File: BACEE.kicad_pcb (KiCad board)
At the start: 2 copper layers, 42.7 x 24.4 mm, 17 parts, among them J2 I2C connector, J3 Digital pins, J4 Serial connector, J5 ICSP connector, U1 24LC1025, U2 DS1337S+, U3 24LC1025, U4 ATMEGA328P-AU, Y1 Crystal32768KHz, Y2 Crystal 16MHz

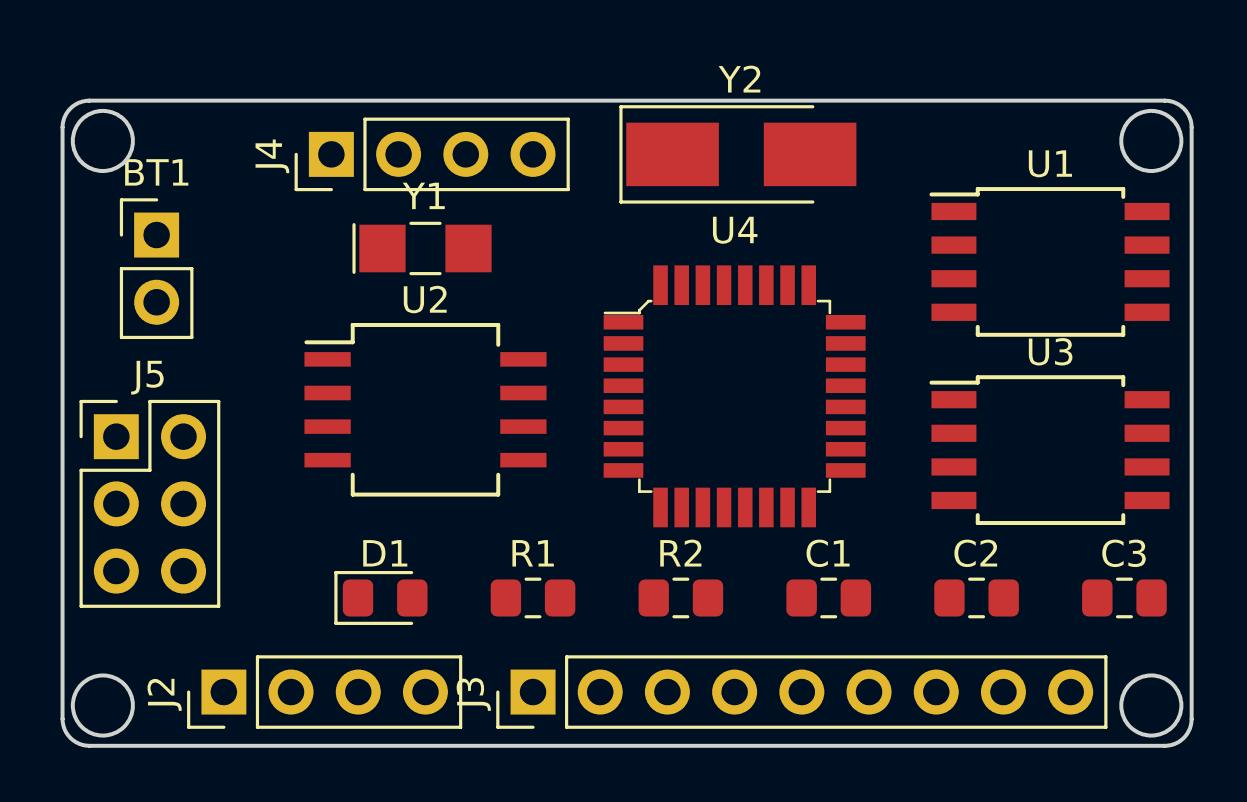
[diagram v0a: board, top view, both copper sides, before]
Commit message: Autorouted 4-layer version.
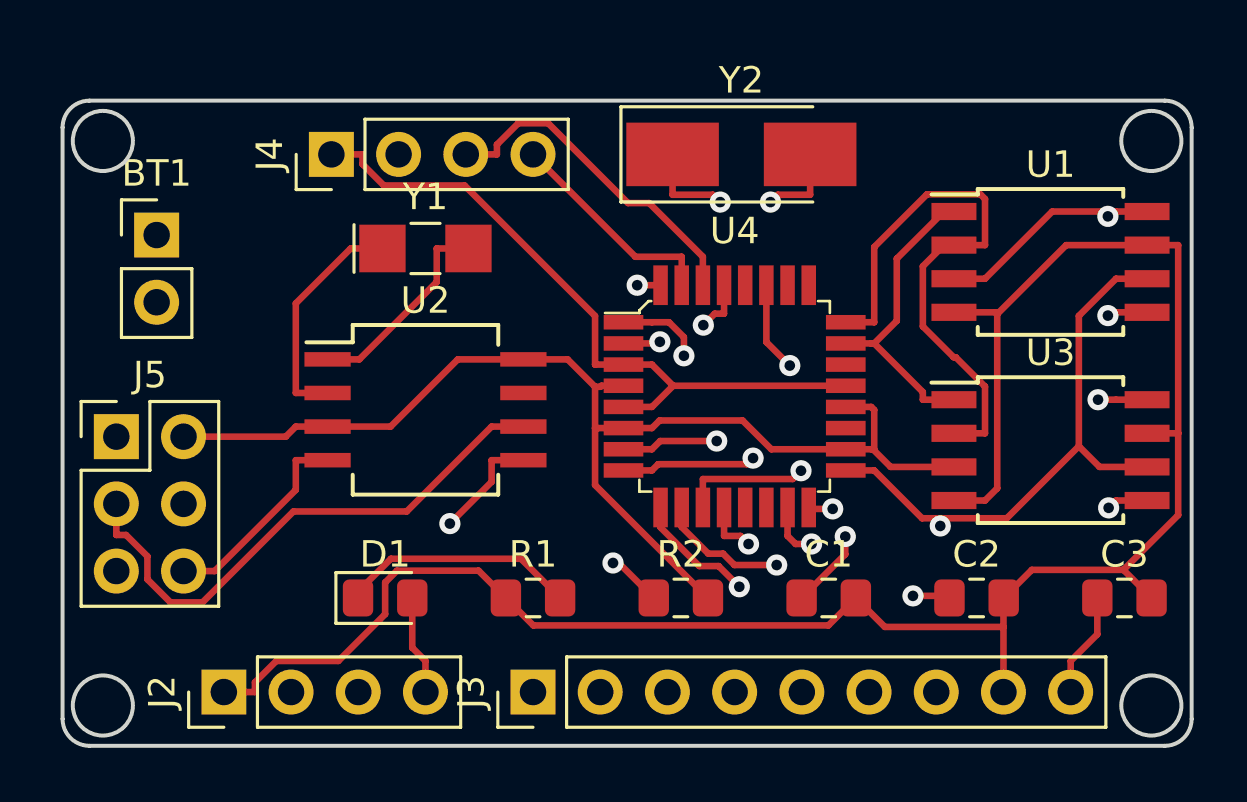
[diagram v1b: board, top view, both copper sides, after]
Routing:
- net /Vcc: track 0.00 -> 147.0 mm, vias 0 -> 2
- net GND: track 0.00 -> 139.8 mm
- net /SCK: track 0.00 -> 87.0 mm, vias 0 -> 1
- net /SDA: track 0.00 -> 59.6 mm, vias 0 -> 4
- net /RESET: track 0.00 -> 35.7 mm, vias 0 -> 2
- net /MISO: track 0.00 -> 29.3 mm, vias 0 -> 1
- net Net-(C2-Pad1): track 0.00 -> 28.8 mm, vias 0 -> 3
- net Net-(C1-Pad1): track 0.00 -> 28.1 mm, vias 0 -> 3
- net /MOSI: track 0.00 -> 26.5 mm, vias 0 -> 1
- net /ADDS2: track 0.00 -> 21.9 mm
- net /D3: track 0.00 -> 21.4 mm, vias 0 -> 1
- net /D2: track 0.00 -> 17.9 mm, vias 0 -> 1
- net /D8: track 0.00 -> 15.8 mm, vias 0 -> 1
- net /D4: track 0.00 -> 14.8 mm, vias 0 -> 1
- net /D7: track 0.00 -> 14.6 mm, vias 0 -> 1
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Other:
- copper layers 2 -> 4

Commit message: Added GND copper fill.
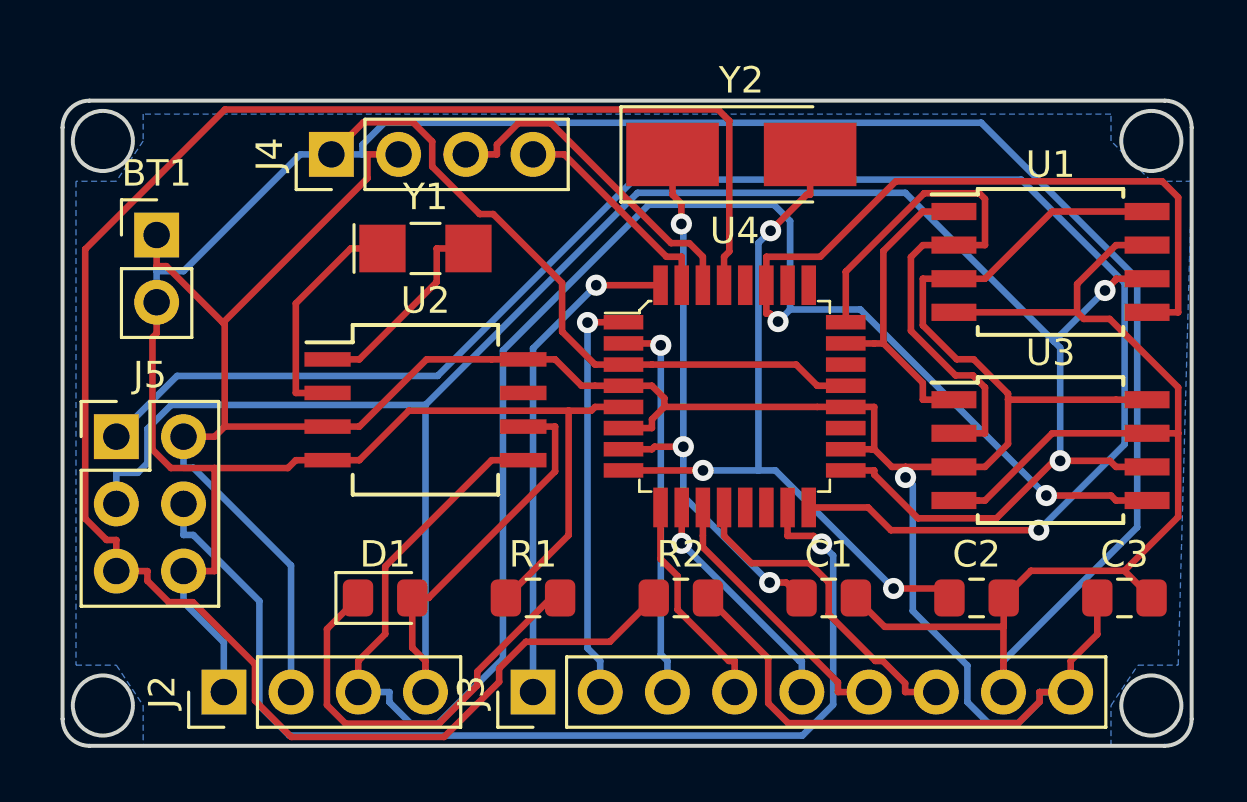
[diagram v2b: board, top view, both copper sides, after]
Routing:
- net GND: track 139.8 -> 176.9 mm
- net /RESET: track 35.7 -> 72.3 mm, vias 2 -> 0
- net /MISO: track 29.3 -> 63.5 mm
- net /SDA: track 59.6 -> 90.0 mm, vias 4 -> 2
- net /Vcc: track 147.0 -> 127.4 mm, vias 2 -> 1
- net /MOSI: track 26.5 -> 40.4 mm
- net Net-(D1-Pad1): track 9.01 -> 15.9 mm
- net Net-(C1-Pad1): track 28.1 -> 21.5 mm
- net /D3: track 21.4 -> 15.5 mm
- net /SCK: track 87.0 -> 91.3 mm, vias 1 -> 2
- net /D7: track 14.6 -> 10.3 mm, vias 1 -> 0
- net /D8: track 15.8 -> 12.4 mm, vias 1 -> 0
- net Net-(C2-Pad1): track 28.8 -> 27.1 mm
- net /D6: track 10.1 -> 8.91 mm
- net /D2: track 17.9 -> 18.8 mm
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- added copper zone on B.Cu, net GND
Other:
- copper layers 4 -> 2

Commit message: Completed silkscreen.
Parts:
- added G***: LOGO, Custom libraries:TE_LOGO_URL_v2, B.Cu at (128.0, 97.8)
- added LOGO_OSHW_silkscreen_2mm: val**, freetronics_footprints:LOGO_OSHW_silkscreen_2mm, F.Cu at (99.6, 92.5)
- added REF**: KiCad-Logo2_8mm_SilkScreen, Symbol:KiCad-Logo2_8mm_SilkScreen, B.Cu at (105.9, 102.9)
- J5: value ICSP connector -> ICSP
- Y1: value Crystal32768KHz -> 32768KHz
- Y2: value Crystal 16MHz -> 16MHz
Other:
- board text added: "Arduino clone with - 2Mbit EEPROM - Clock & calendar - I2C, SPI & GPIOs"
- board text added: "C"
- board text added: "D2"
- board text added: "D3"
- board text added: "D4"
- board text added: "D6"
- board text added: "D7"
- board text added: "D8"
- board text added: "Designed by Peter in Berowra"
- board text added: "GND"
- board text added: "MISO"
- board text added: "MOSI"
- board text added: "RST"
- board text added: "RX"
- board text added: "SCK"
- board text added: "SDA"
- board text added: "TX"
- board text added: "Vcc"
